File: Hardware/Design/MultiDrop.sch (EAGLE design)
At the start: 12 parts

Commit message: readme
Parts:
- added D1, D2: (no value), D-SBR:DSMB
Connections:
- removed net N$31: U$3.BAT, U$7.BAT_PWR
- removed net N$34: PV4.PV_PWR, U$3.PV
- removed net N$36: PV2.PV_PWR, U$5.PV
- new net N$12: D1.A, PV2.PV_PWR
- new net N$15: D1.K, U$5.PWR, U$9.BAT_PWR
- new net N$16: D2.A, PV4.PV_PWR
- net N$17: now also D2.K, U$3.PWR, U$7.BAT_PWR; no longer U$5.BAT, U$9.BAT_PWR
- net N$3: now also PM1.TX; no longer PM1.RX

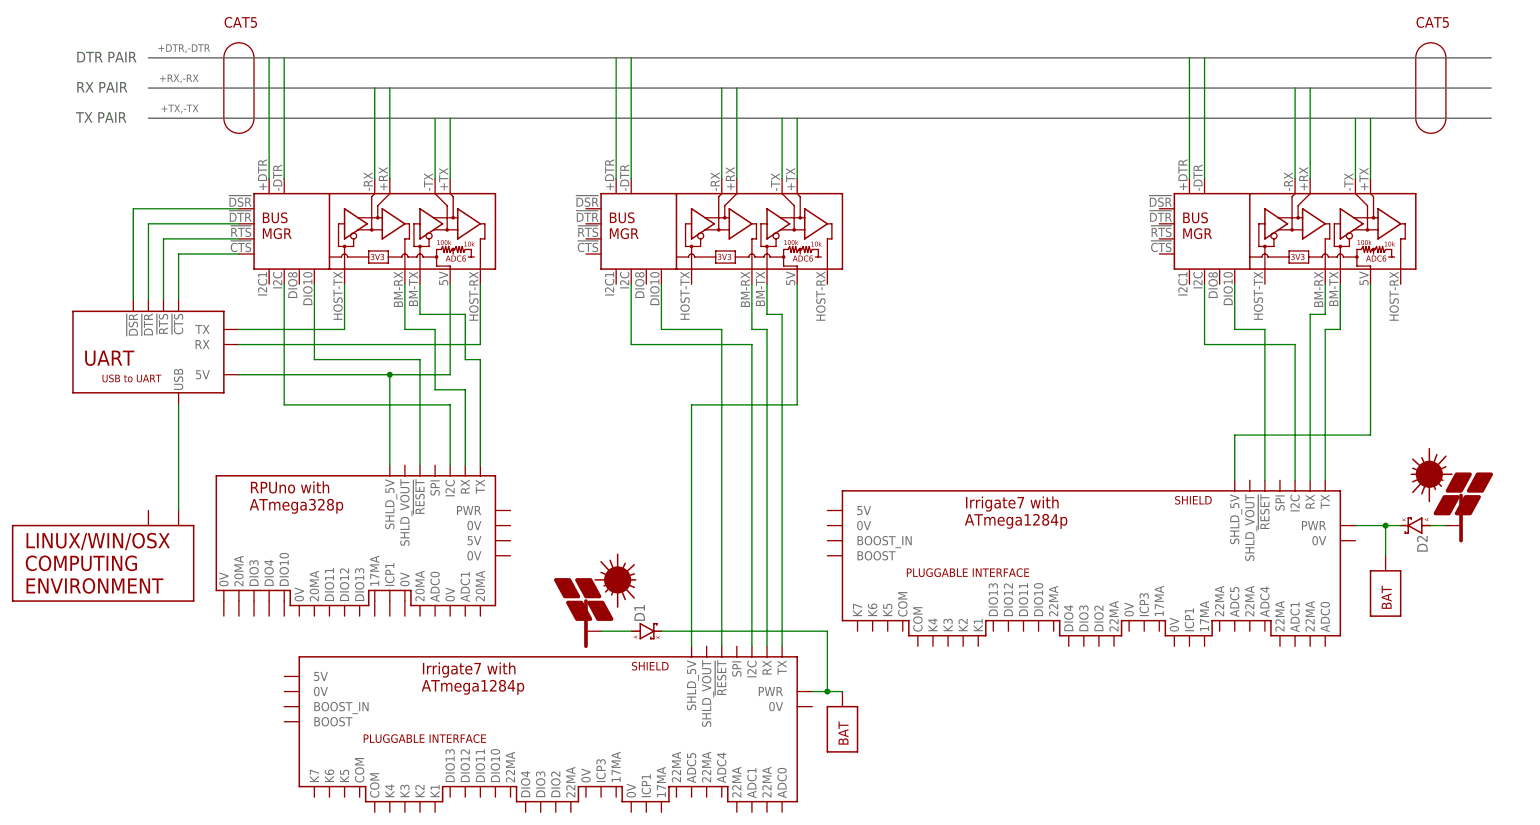
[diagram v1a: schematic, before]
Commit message: Hardware: ^6 changes lots, but the RS-422 as a remote should not have changed
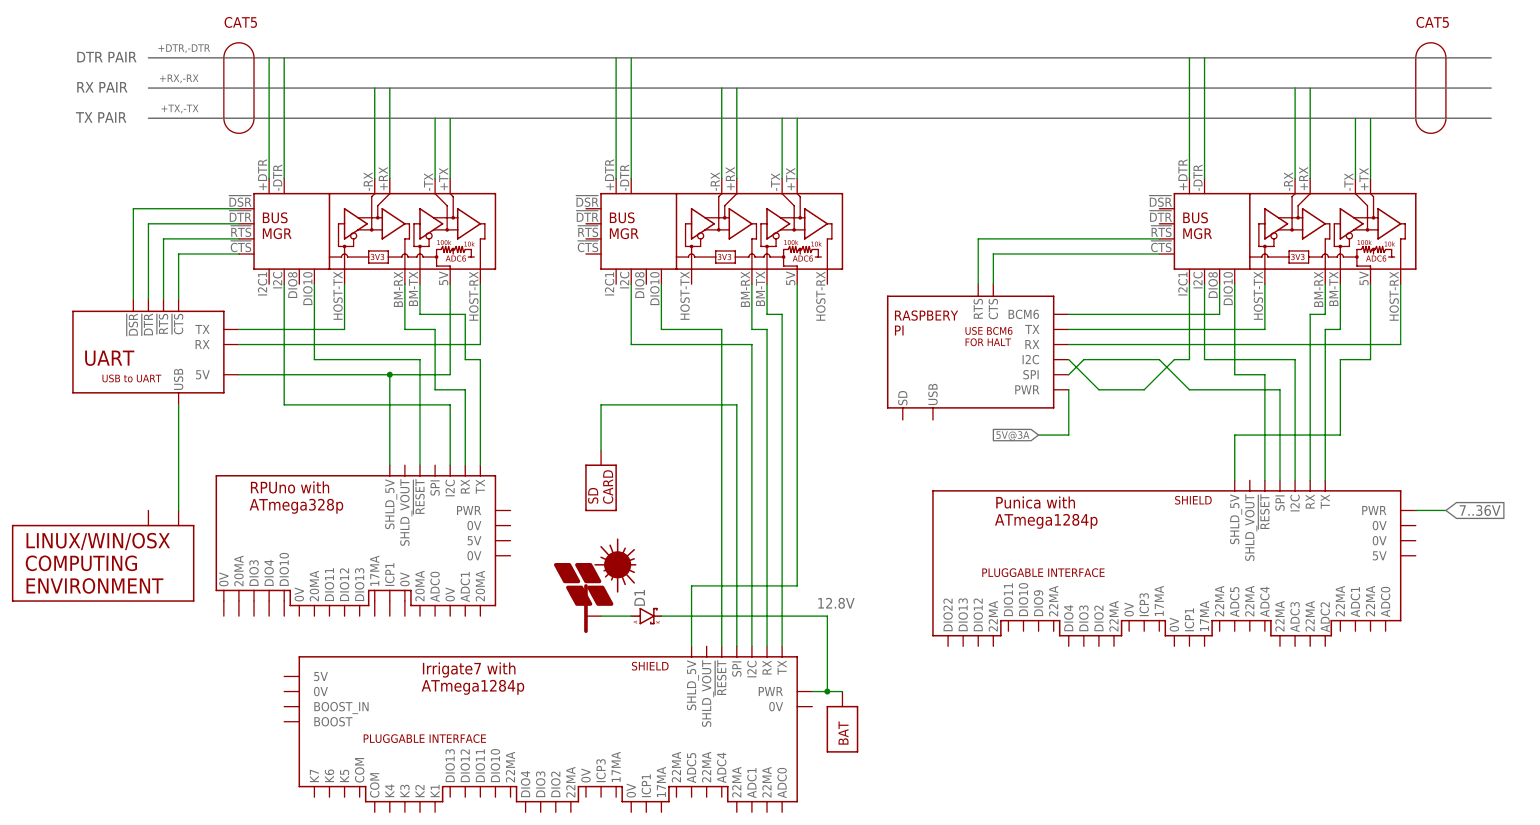
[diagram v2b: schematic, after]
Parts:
- removed D2: (no value), D-SBR:DSMB
- removed PV4: PV, Documentation:PV
- removed U$7: BAT, Documentation:BAT
- added SD1: SD, Documentation:SD
- added U$6: PUNICA, Documentation:PUNICA
- U$3: value IRRIGATE7 -> PI; device Documentation:IRRIGATE7 -> Documentation:PI
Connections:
- net N$15 renamed 12.8V
- removed net N$16: D2.A, PV4.PV_PWR
- removed net N$17: D2.K, U$3.PWR, U$7.BAT_PWR
- new net 5V@3A: U$3.PWR
- new net 7..36V: U$6.PWR
- new net N$18: SD1.PV_PWR, U$5.SPI
- new net N$19: U$1.!CTS, U$3.CTS
- new net N$20: U$1.!RTS, U$3.RTS
- new net N$22: U$1.I2C1, U$3.I2C
- new net N$23: U$1.DIO8, U$3.BCM6
- new net N$24: U$1.HOST_TX, U$3.TX
- new net N$25: U$1.HOST_RX, U$3.RX
- new net N$26: U$3.SPI, U$6.SPI
- net N$13: now also U$6.SHLD_5V; no longer U$3.SHLD_5V
- net N$14: now also U$6.TX; no longer U$3.TX
- net N$21: now also U$6.RX; no longer U$3.RX
- net N$32: now also U$6.I2C; no longer U$3.I2C
- net N$43: now also U$6.!RESET; no longer U$3.!RESET
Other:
- note added: "10AHr SLA 12V AGM CHARGING AT LESS THAN 0.02C"
- note added: "Adafruit product/254"
- note added: "IOFF"
- note added: "IOFF allows power off without pulling down connecting lines"
- note added: "SLP003-12U"
- note added: "SPI FROM MSTR"
- note added: "SPI TO SLV"
- moved on the sheet: D1

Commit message: Remote: add twi1 /w commands 0, 2, 3, 6, 7 for host use
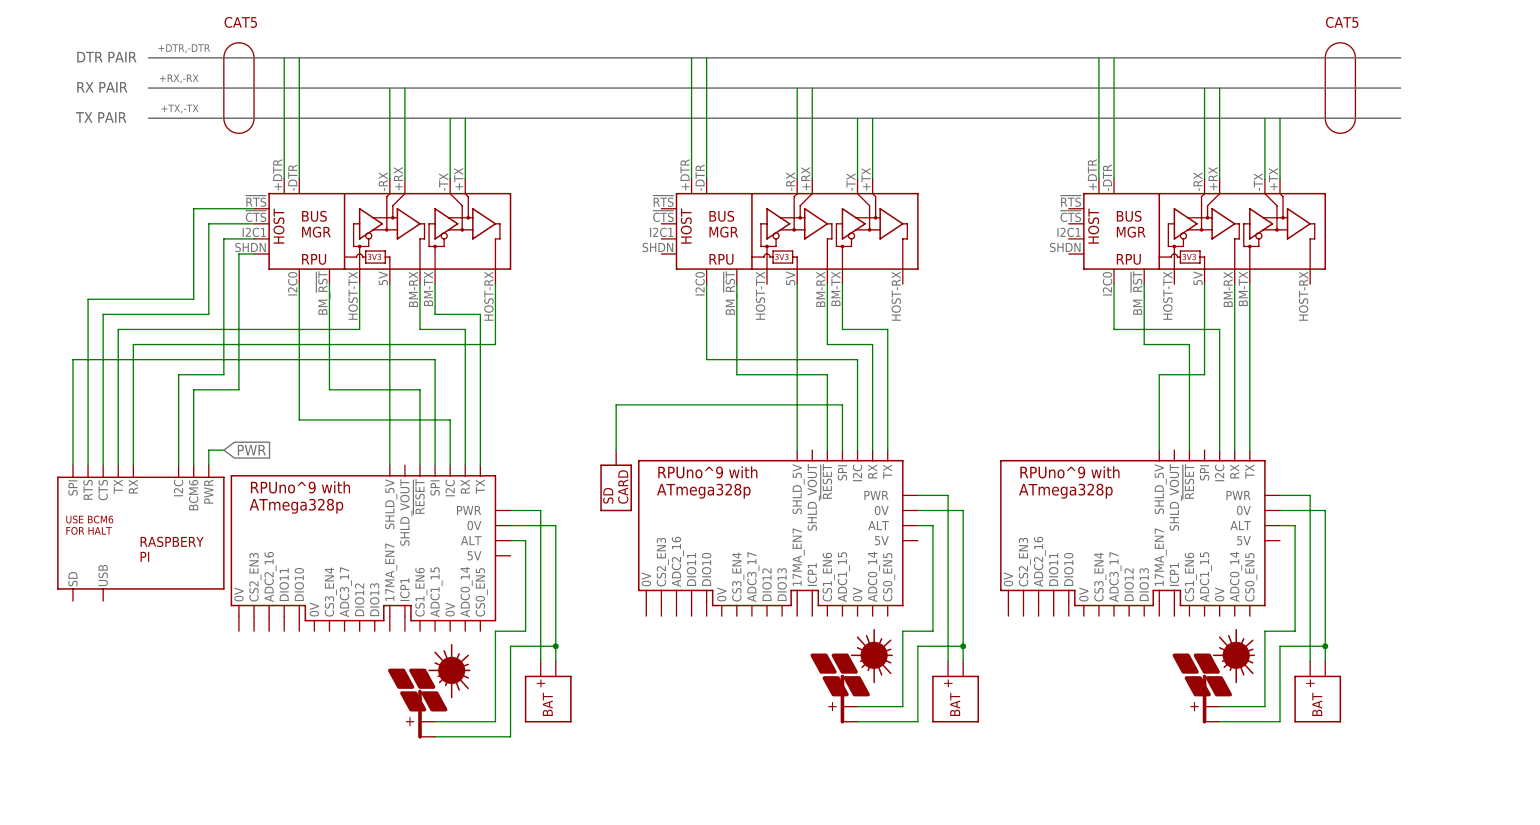
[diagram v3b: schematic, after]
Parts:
- removed D1: (no value), D-SBR:DSMB
- removed PM1: (no value), Documentation:DESKTOP
- removed U$6: PUNICA, Documentation:PUNICA
- removed UART1: (no value), Documentation:UART
- added BM1, BM3: (no value), Documentation:RPUNO
- added PV1, PV3: PV, Documentation:PV
- added U$7: PI, Documentation:PI
- U$3: value PI -> BAT; device Documentation:PI -> Documentation:BAT
- U$5: value IRRIGATE7 -> BAT; device Documentation:IRRIGATE7 -> Documentation:BAT
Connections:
- removed net 12.8V: D1.K, U$5.PWR, U$9.BAT_PWR
- removed net 5V@3A: U$3.PWR
- removed net 7..36V: U$6.PWR
- removed net N$20: U$1.!RTS, U$3.RTS
- removed net N$23: U$1.DIO8, U$3.BCM6
- new net N$15: BM2.0V@2, PV2.-PV, U$9.-BAT
- new net N$16: BM1.ALT, PV1.+PV
- new net N$17: BM2.ALT, PV2.+PV
- new net PWR: U$7.PWR
- net +DTR: now also U$1.+DTR; no longer U$4.+DTR
- net +DTR3: now also U$4.+DTR; no longer U$1.+DTR
- net +RX: now also U$1.+RX; no longer U$4.+RX
- net +RX3: now also U$4.+RX; no longer U$1.+RX
- net +TX: now also U$1.+TX; no longer U$4.+TX
- net +TX3: now also U$4.+TX; no longer U$1.+TX
- net -DTR: now also U$1.-DTR; no longer U$4.-DTR
- net -DTR3: now also U$4.-DTR; no longer U$1.-DTR
- net -RX: now also U$1.-RX; no longer U$4.-RX
- net -RX3: now also U$4.-RX; no longer U$1.-RX
- net -TX: now also U$1.-TX; no longer U$4.-TX
- net -TX3: now also U$4.-TX; no longer U$1.-TX
- net N$1: now also U$1.BM_TX; no longer U$4.BM_TX
- net N$10: now also BM1.TX; no longer U$5.TX
- net N$11: now also BM1.RX; no longer U$5.RX
- net N$12: now also BM2.PWR, U$9.+BAT; no longer D1.A, PV2.PV_PWR
- net N$13: now also BM3.SHLD_5V, U$4.PWR; no longer U$1.PWR, U$6.SHLD_5V
- net N$14: now also BM3.TX, U$4.BM_TX; no longer U$1.BM_TX, U$6.TX
- net N$18: now also BM1.SPI; no longer U$5.SPI
- net N$19: now also BM1.0V@2, PV1.-PV, U$3.-BAT; no longer U$1.!CTS, U$3.CTS
- net N$2: now also U$1.BM_RX; no longer U$4.BM_RX
- net N$21: now also BM3.RX, U$4.BM_RX; no longer U$1.BM_RX, U$6.RX
- net N$22: now also BM1.PWR, U$3.+BAT; no longer U$1.I2C1, U$3.I2C
- net N$24: now also BM3.ALT, PV3.+PV; no longer U$1.HOST_TX, U$3.TX
- net N$25: now also BM3.0V@2, PV3.-PV, U$5.-BAT; no longer U$1.HOST_RX, U$3.RX
- net N$26: now also BM3.PWR, U$5.+BAT; no longer U$3.SPI, U$6.SPI
- net N$29: now also U$1.PWR; no longer U$4.PWR, UART1.5V
- net N$3: now also BM2.SPI, U$7.SPI; no longer PM1.TX, UART1.USB
- net N$30: now also U$1.BM-!RST!; no longer U$4.DIO10
- net N$32: now also BM3.I2C, U$4.I2C0; no longer U$1.I2C, U$6.I2C
- net N$33: now also U$1.I2C0; no longer U$4.I2C
- net N$4: now also U$1.!CTS, U$7.CTS; no longer U$4.!CTS, UART1.!CTS
- net N$43: now also BM3.!RESET, U$4.BM-!RST!; no longer U$1.DIO10, U$6.!RESET
- net N$44: now also BM1.!RESET, U$2.BM-!RST!; no longer U$2.DIO10, U$5.!RESET
- net N$45: now also BM1.SHLD_5V; no longer U$5.SHLD_5V
- net N$48: now also BM1.I2C, U$2.I2C0; no longer U$2.I2C, U$5.I2C
- net N$5: now also U$1.!RTS, U$7.RTS; no longer U$4.!RTS, UART1.!RTS
- net N$6: now also U$1.SHDN, U$7.BCM6; no longer U$4.!DTR, UART1.!DTR
- net N$7: now also U$1.I2C1, U$7.I2C; no longer U$4.!DSR, UART1.!DSR
- net N$8: now also U$1.HOST_RX, U$7.RX; no longer U$4.HOST_RX, UART1.RX
- net N$9: now also U$1.HOST_TX, U$7.TX; no longer U$4.HOST_TX, UART1.TX
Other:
- note added: "20AHr SLA 12V AGM CHARGING AT LESS THAN 0.1C"
- note added: "IOFF allows SBC to power off without pulling down connected lines"
- note added: "SLP020-12U"
- note removed: "10AHr SLA 12V AGM CHARGING AT LESS THAN 0.02C"
- note removed: "IOFF allows power off without pulling down connecting lines"
- note removed: "RPUftdi"
- note removed: "SPI FROM MSTR"
